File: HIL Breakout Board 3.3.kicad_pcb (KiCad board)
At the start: 6 copper layers, 262.5 x 110.1 mm, 36 parts, among them J1 DIN41612_03x32_C_Split, J2 DIN41612_03x32_C_Split, J4 2-5174225-5, J5 2-5174225-5

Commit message: Added traces from all switches to NI connector
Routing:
- net (no net): track 0.00 -> 500.6 mm
- net Net-(J4-PadB13): track 0.00 -> 307.5 mm, vias 0 -> 2
- net Net-(J4-PadB12): track 0.00 -> 292.3 mm
- net Net-(J4-PadA13): track 0.00 -> 282.9 mm, vias 0 -> 2
- net Net-(J4-PadA12): track 0.00 -> 261.1 mm, vias 0 -> 2
- net Net-(J4-PadB11): track 0.00 -> 252.6 mm, vias 0 -> 2
- net Net-(J4-PadA11): track 0.00 -> 228.7 mm, vias 0 -> 2
- net Net-(J4-PadB10): track 0.00 -> 224.9 mm, vias 0 -> 1
- net Net-(J4-PadA10): track 0.00 -> 198.0 mm, vias 0 -> 2
- net Net-(J5-PadB10): track 0.00 -> 169.5 mm, vias 0 -> 1
- net Net-(J4-PadB9): track 0.00 -> 168.6 mm, vias 0 -> 2
- net DI16: track 0.00 -> 159.4 mm
- net DO16: track 0.00 -> 159.1 mm
- net DI0: track 0.00 -> 159.0 mm
- net Net-(J4-PadB8): track 0.00 -> 158.9 mm, vias 0 -> 1
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
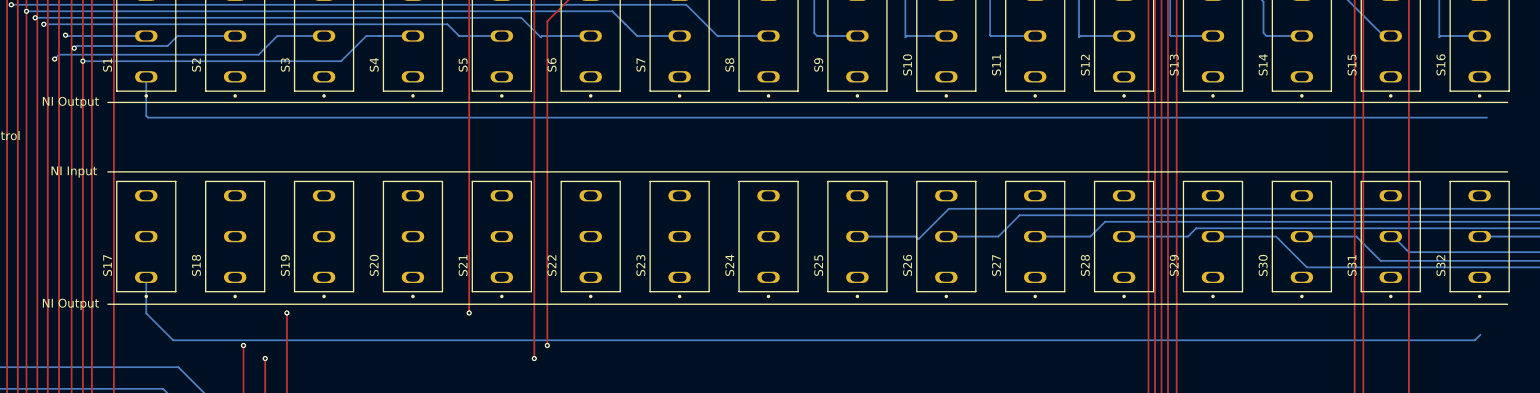
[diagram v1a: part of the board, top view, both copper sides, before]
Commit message: Added all NI input signals to switches
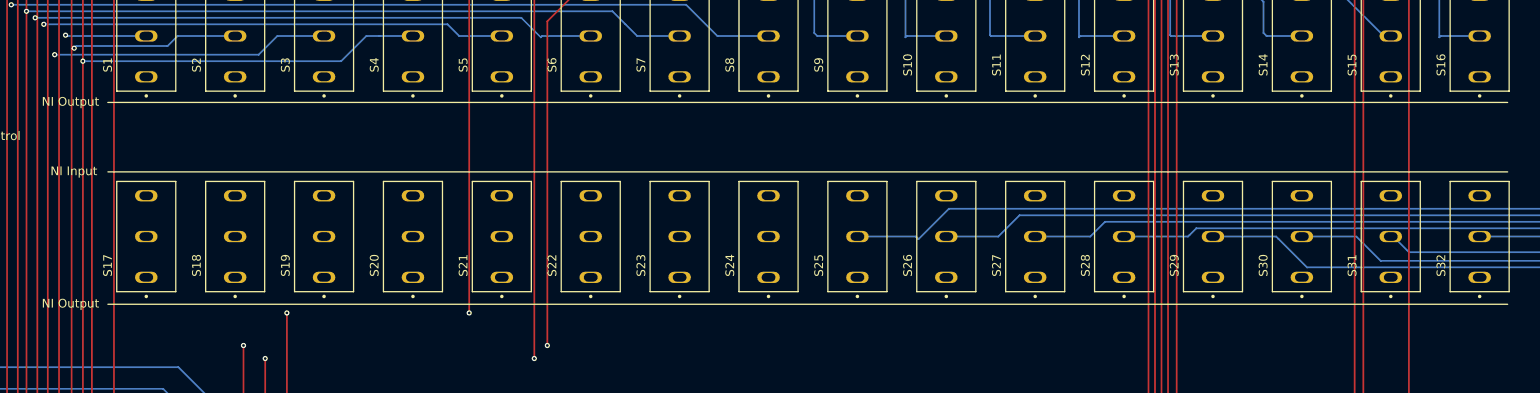
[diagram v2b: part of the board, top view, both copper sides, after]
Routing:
- net DO17: track 0.00 -> 202.2 mm
- net DO18: track 0.00 -> 193.0 mm
- net DO19: track 0.00 -> 182.8 mm
- net DO20: track 0.00 -> 172.4 mm
- net DO21: track 0.00 -> 162.1 mm
- net DI16: track 159.4 -> 0.00 mm
- net DI0: track 159.0 -> 0.00 mm
- net DO22: track 0.00 -> 152.0 mm
- net DO23: track 0.00 -> 144.4 mm
- net DO24: track 0.00 -> 134.2 mm
- net DO1: track 0.00 -> 125.1 mm
- net DO25: track 0.00 -> 124.9 mm
- net DO2: track 0.00 -> 116.5 mm
- net DO26: track 0.00 -> 116.1 mm
- net DO27: track 0.00 -> 106.8 mm
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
